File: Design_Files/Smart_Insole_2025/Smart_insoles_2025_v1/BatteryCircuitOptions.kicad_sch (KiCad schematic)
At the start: 2 parts, among them J2 Conn_01x02_Pin

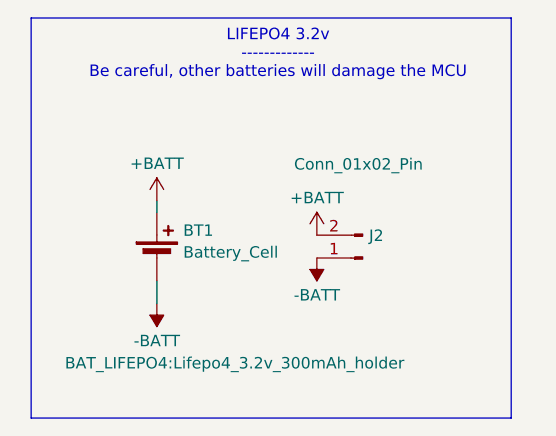
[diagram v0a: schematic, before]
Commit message: Added different AFE circuits to the schematic. Needs verification
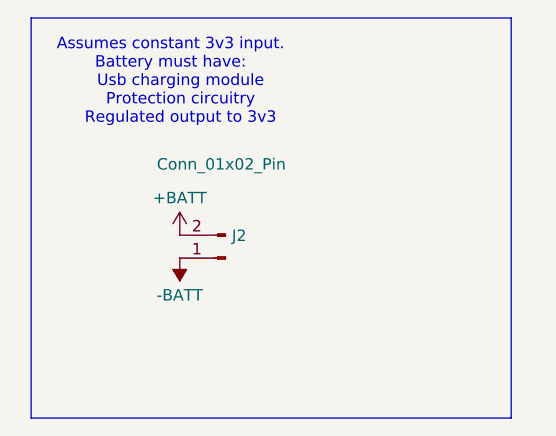
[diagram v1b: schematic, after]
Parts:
- removed BT1: Battery_Cell, BAT_LIFEPO4:Lifepo4_3.2v_300mAh_holder, symbol Device:Battery_Cell
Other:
- note added: "Assumes constant 3v3 input. Battery must have: Usb charging module Protection circuitry Regulated output to 3v3"
- note removed: "LIFEPO4 3.2v ------------- Be careful, other batteries will damage the MCU"
- moved on the sheet: J2

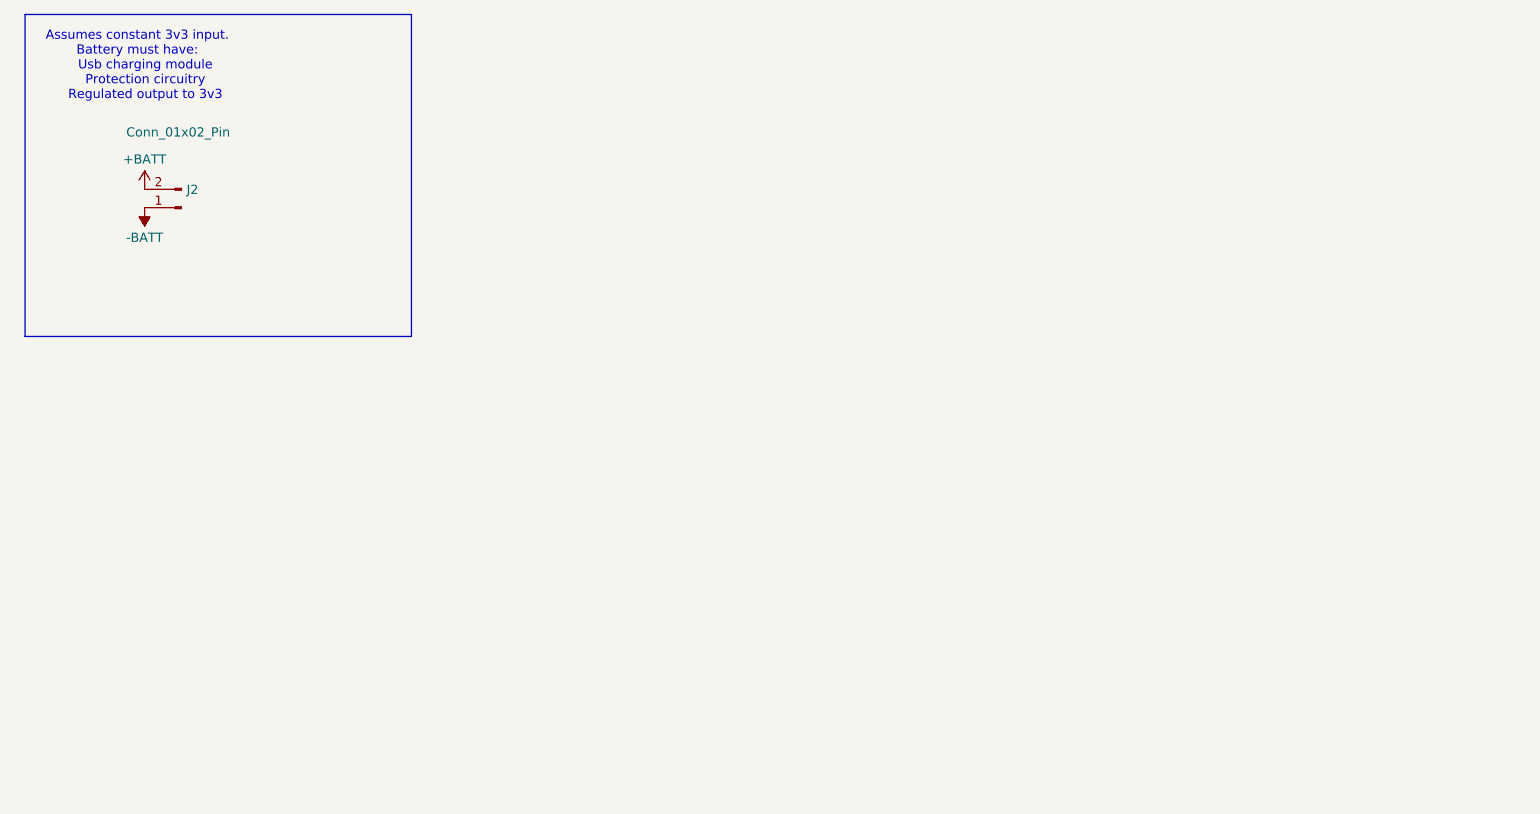
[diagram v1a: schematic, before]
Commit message: Project division to account for multiple AFE conditioning circuit
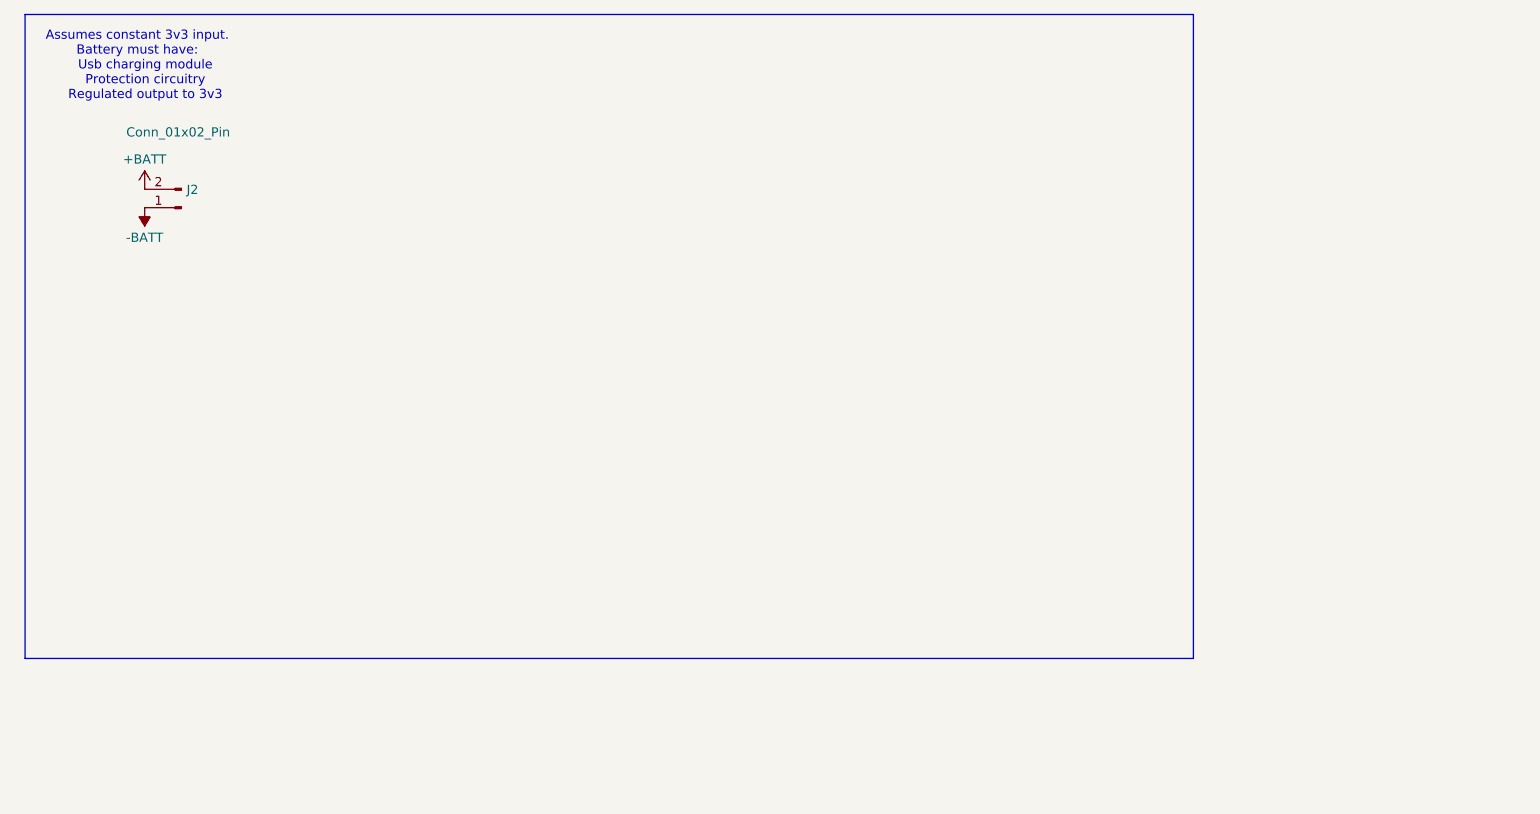
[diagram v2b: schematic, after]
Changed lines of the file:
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@@
 	(rectangle
 		(start 24.13 19.05)
-		(end 77.47 63.5)
+		(end 185.42 107.95)
 		(stroke
 			(width 0)

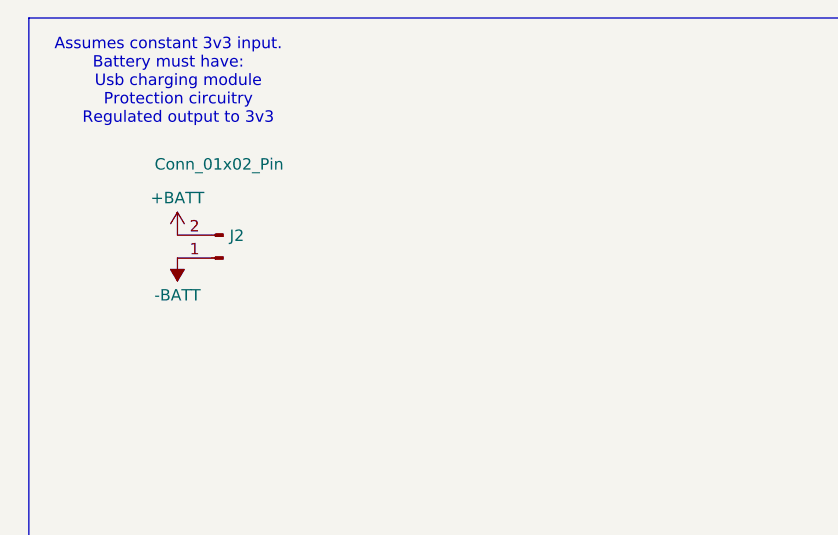
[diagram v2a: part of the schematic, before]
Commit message: Added battery connector footprint. Grouping componnets in PcbNew
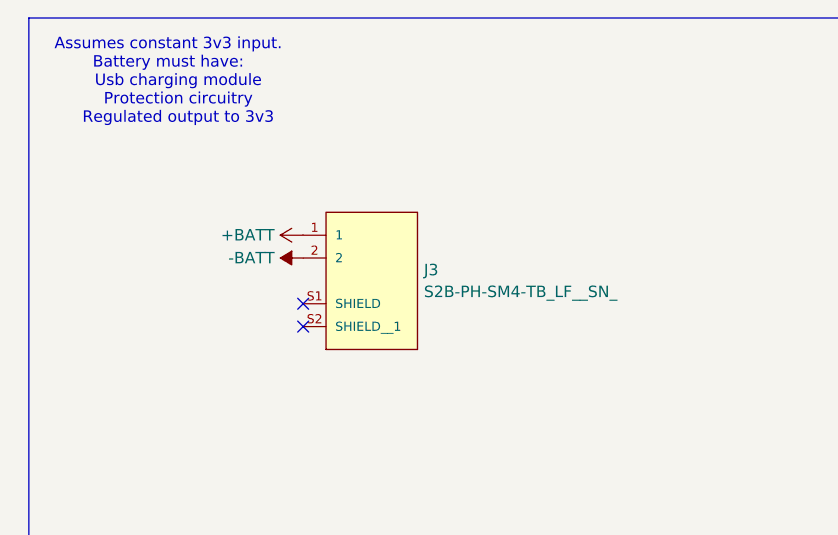
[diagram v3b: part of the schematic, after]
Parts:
- removed J2: Conn_01x02_Pin, Connector_JST:JST_EH_S2B-EH_1x02_P2.50mm_Horizontal, symbol Connector:Conn_01x02_Pin
- added J3: S2B-PH-SM4-TB_LF__SN_, JST-PH2-2.00MM-SMD-HORIZONTAL:JST_S2B-PH-SM4-TB_LF__SN_, symbol S2B-PH-SM4-TB_LF__SN_:S2B-PH-SM4-TB_LF__SN_
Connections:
- net +BATT: now also J3.1
- net -BATT: now also J3.2
- no-connect marks 0 -> 2
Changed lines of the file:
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@@
 	(generator_version "8.0")
 	(paper "A4")
+	(no_connect
+		(at 54.61 50.8)
+	)
+	(no_connect
+		(at 54.61 53.34)
+	)
 	(rectangle
 		(start 24.13 19.05)
@@
 	)
 	(symbol
-		(lib_id "Connector:Conn_01x02_Pin")
-		(at 45.72 45.72 180)
+		(lib_id "power:+BATT")
+		(at 54.61 43.18 90)
 		(unit 1)
 		(exclude_from_sim no)
@@
 		(on_board yes)
 		(dnp no)
-		(property "Reference" "J2"
-			(at 46.4312 43.2378 0)
-			(effects
-				(font
-					(size 1.27 1.27)
-				)
-				(justify right)
-			)
-		)
-		(property "Value" "Conn_01x02_Pin"
-			(at 38.1 35.306 0)
-			(effects
-				(font
-					(size 1.27 1.27)
-				)
-				(justify right)
-			)
-		)
-		(property "Footprint" "Connector_JST:JST_EH_S2B-EH_1x02_P2.50mm_Horizontal"
-			(at 45.72 45.72 0)
-			(effects
-				(font
-					(size 1.27 1.27)
-				)
-				(hide yes)
-			)
-		)
-		(property "Datasheet" "~"
-			(at 45.72 45.72 0)
-			(effects
-				(font
-					(size 1.27 1.27)
-				)
-				(hide yes)
-			)
-		)
-		(property "Description" "Generic connector, single row, 01x02, script generated"
-			(at 45.72 45.72 0)
+		(fields_autoplaced yes)
+		(property "Reference" "#PWR022"
+			(at 58.42 43.18 0)
+			(effects
+				(font
+					(size 1.27 1.27)
+				)
+				(hide yes)
+			)
+		)
+		(property "Value" "+BATT"
+			(at 51.435 43.18 90)
+			(effects
+				(font
+					(size 1.27 1.27)
+				)
+				(justify left)
+			)
+		)
+		(property "Footprint" ""
+			(at 54.61 43.18 0)
+			(effects
+				(font
+					(size 1.27 1.27)
+				)
+				(hide yes)
+			)
+		)
+		(property "Datasheet" ""
+			(at 54.61 43.18 0)
+			(effects
+				(font
+					(size 1.27 1.27)
+				)
+				(hide yes)
+			)
+		)
+		(property "Description" "Power symbol creates a global label with name \"+BATT\""
+			(at 54.61 43.18 0)
 			(effects
 				(font
@@
 		)
 		(pin "1"
-		)
-		(pin "2"
 		)
 		(instances
 			(project "Smart_insoles_2025_v1"
 				(path "/f1f3d712-154d-4111-a7c4-f47541abccf8/720d2e8f-49b8-46ab-8d82-07d24ffc5c73"
-					(reference "J2")
+					(reference "#PWR022")
 					(unit 1)
 				)
@@
 	(symbol
 		(lib_id "power:-BATT")
-		(at 40.64 45.72 180)
+		(at 54.61 45.72 90)
 		(unit 1)
 		(exclude_from_sim no)
@@
 		(fields_autoplaced yes)
 		(property "Reference" "#PWR023"
-			(at 40.64 41.91 0)
+			(at 58.42 45.72 0)
 			(effects
 				(font
@@
 		)
 		(property "Value" "-BATT"
-			(at 40.64 49.8531 0)
-			(effects
-				(font
-					(size 1.27 1.27)
-				)
+			(at 51.435 45.72 90)
+			(effects
+				(font
+					(size 1.27 1.27)
+				)
+				(justify left)
 			)
 		)
 		(property "Footprint" ""
-			(at 40.64 45.72 0)
+			(at 54.61 45.72 0)
 			(effects
 				(font
@@
 		)
 		(property "Datasheet" ""
-			(at 40.64 45.72 0)
+			(at 54.61 45.72 0)
 			(effects
 				(font
@@
 		)
 		(property "Description" "Power symbol creates a global label with name \"-BATT\""
-			(at 40.64 45.72 0)
+			(at 54.61 45.72 0)
 			(effects
 				(font
@@
 	)
 	(symbol
-		(lib_id "power:+BATT")
-		(at 40.64 43.18 0)
+		(lib_id "S2B-PH-SM4-TB_LF__SN_:S2B-PH-SM4-TB_LF__SN_")
+		(at 62.23 45.72 0)
 		(unit 1)
 		(exclude_from_sim no)
@@
 		(dnp no)
 		(fields_autoplaced yes)
-		(property "Reference" "#PWR022"
-			(at 40.64 46.99 0)
-			(effects
-				(font
-					(size 1.27 1.27)
-				)
-				(hide yes)
-			)
-		)
-		(property "Value" "+BATT"
-			(at 40.64 39.0469 0)
-			(effects
-				(font
-					(size 1.27 1.27)
-				)
-			)
-		)
-		(property "Footprint" ""
-			(at 40.64 43.18 0)
-			(effects
-				(font
-					(size 1.27 1.27)
-				)
+		(property "Reference" "J3"
+			(at 68.0212 47.0478 0)
+			(effects
+				(font
+					(size 1.27 1.27)
+				)
+				(justify left)
+			)
+		)
+		(property "Value" "S2B-PH-SM4-TB_LF__SN_"
+			(at 68.0212 49.4721 0)
+			(effects
+				(font
+					(size 1.27 1.27)
+				)
+				(justify left)
+			)
+		)
+		(property "Footprint" "JST-PH2-2.00MM-SMD-HORIZONTAL:JST_S2B-PH-SM4-TB_LF__SN_"
+			(at 62.23 45.72 0)
+			(effects
+				(font
+					(size 1.27 1.27)
+				)
+				(justify bottom)
 				(hide yes)
 			)
 		)
 		(property "Datasheet" ""
-			(at 40.64 43.18 0)
-			(effects
-				(font
-					(size 1.27 1.27)
-				)
-				(hide yes)
-			)
-		)
-		(property "Description" "Power symbol creates a global label with name \"+BATT\""
-			(at 40.64 43.18 0)
-			(effects
-				(font
-					(size 1.27 1.27)
-				)
+			(at 62.23 45.72 0)
+			(effects
+				(font
+					(size 1.27 1.27)
+				)
+				(hide yes)
+			)
+		)
+		(property "Description" ""
+			(at 62.23 45.72 0)
+			(effects
+				(font
+					(size 1.27 1.27)
+				)
+				(hide yes)
+			)
+		)
+		(property "MF" "JST Sales"
+			(at 62.23 45.72 0)
+			(effects
+				(font
+					(size 1.27 1.27)
+				)
+				(justify bottom)
+				(hide yes)
+			)
+		)
+		(property "Description_1" "\n                        \n                            Connector Header Surface Mount, Right Angle 2 position 0.079 (2.00mm)\n                        \n"
+			(at 62.23 45.72 0)
+			(effects
+				(font
+					(size 1.27 1.27)
+				)
+				(justify bottom)
+				(hide yes)
+			)
+		)
+		(property "Package" "None"
+			(at 62.23 45.72 0)
+			(effects
+				(font
+					(size 1.27 1.27)
+				)
+				(justify bottom)
+				(hide yes)
+			)
+		)
+		(property "Price" "None"
+			(at 62.23 45.72 0)
+			(effects
+				(font
+					(size 1.27 1.27)
+				)
+				(justify bottom)
+				(hide yes)
+			)
+		)
+		(property "Check_prices" "https://www.snapeda.com/parts/S2B-PH-SM4-TB(LF)(SN)/JST/view-part/?ref=eda"
+			(at 62.23 45.72 0)
+			(effects
+				(font
+					(size 1.27 1.27)
+				)
+				(justify bottom)
+				(hide yes)
+			)
+		)
+		(property "STANDARD" "Manufacturer Recommendation"
+			(at 62.23 45.72 0)
+			(effects
+				(font
+					(size 1.27 1.27)
+				)
+				(justify bottom)
+				(hide yes)
+			)
+		)
+		(property "SnapEDA_Link" "https://www.snapeda.com/parts/S2B-PH-SM4-TB(LF)(SN)/JST/view-part/?ref=snap"
+			(at 62.23 45.72 0)
+			(effects
+				(font
+					(size 1.27 1.27)
+				)
+				(justify bottom)
+				(hide yes)
+			)
+		)
+		(property "MP" "S2B-PH-SM4-TB(LF)(SN)"
+			(at 62.23 45.72 0)
+			(effects
+				(font
+					(size 1.27 1.27)
+				)
+				(justify bottom)
+				(hide yes)
+			)
+		)
+		(property "Availability" "In Stock"
+			(at 62.23 45.72 0)
+			(effects
+				(font
+					(size 1.27 1.27)
+				)
+				(justify bottom)
+				(hide yes)
+			)
+		)
+		(property "MANUFACTURER" "JST"
+			(at 62.23 45.72 0)
+			(effects
+				(font
+					(size 1.27 1.27)
+				)
+				(justify bottom)
 				(hide yes)
 			)
 		)
 		(pin "1"
+		)
+		(pin "2"
+		)
+		(pin "S2"
+		)
+		(pin "S1"
 		)
 		(instances
 			(project "Smart_insoles_2025_v1"
 				(path "/f1f3d712-154d-4111-a7c4-f47541abccf8/720d2e8f-49b8-46ab-8d82-07d24ffc5c73"
-					(reference "#PWR022")
+					(reference "J3")
 					(unit 1)
 				)

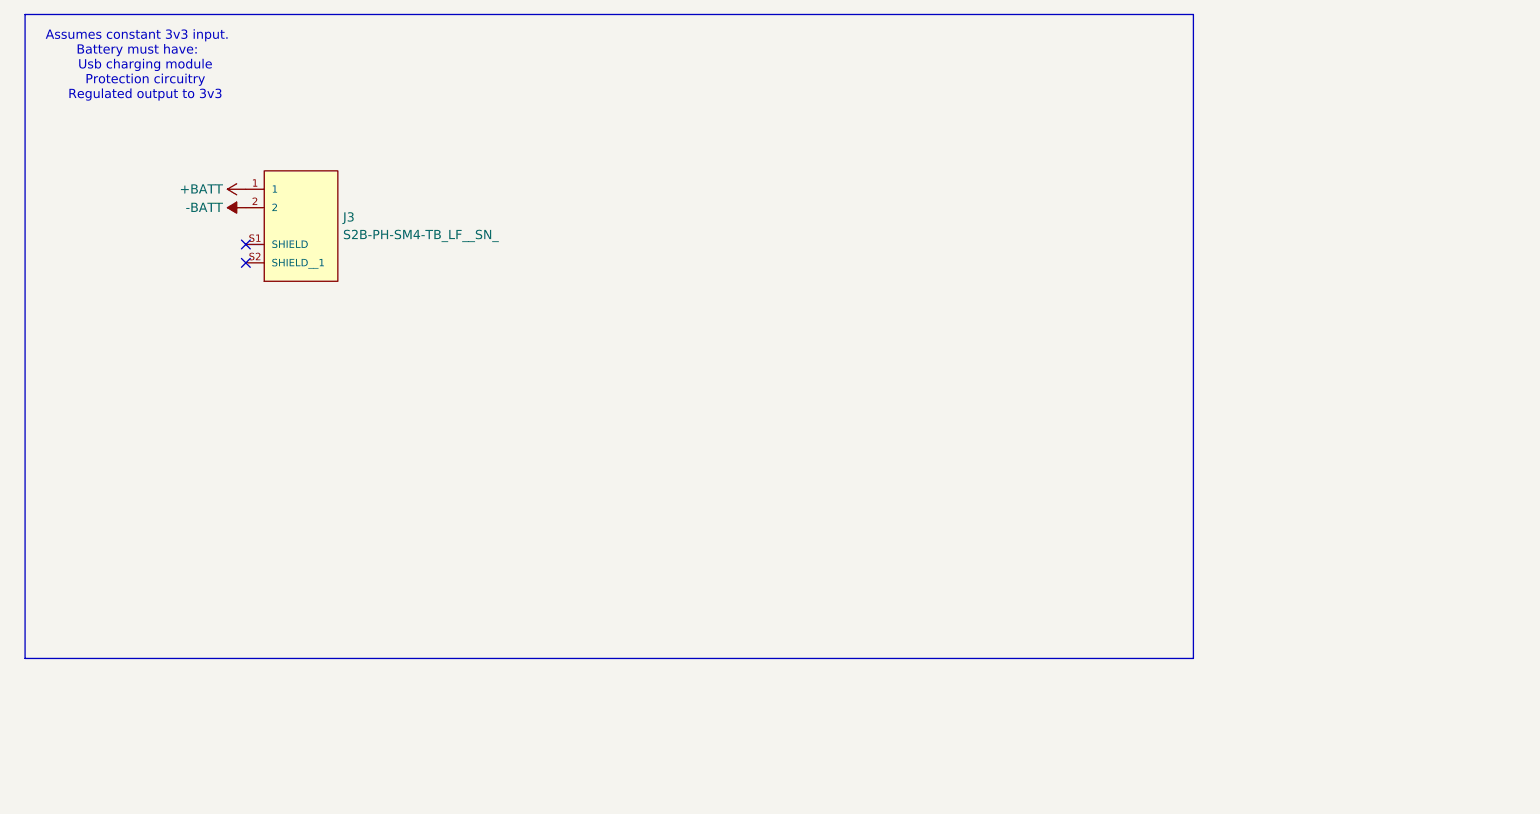
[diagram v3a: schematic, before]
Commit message: PCBnew:Moving placed components. Fixed REF of mcp component
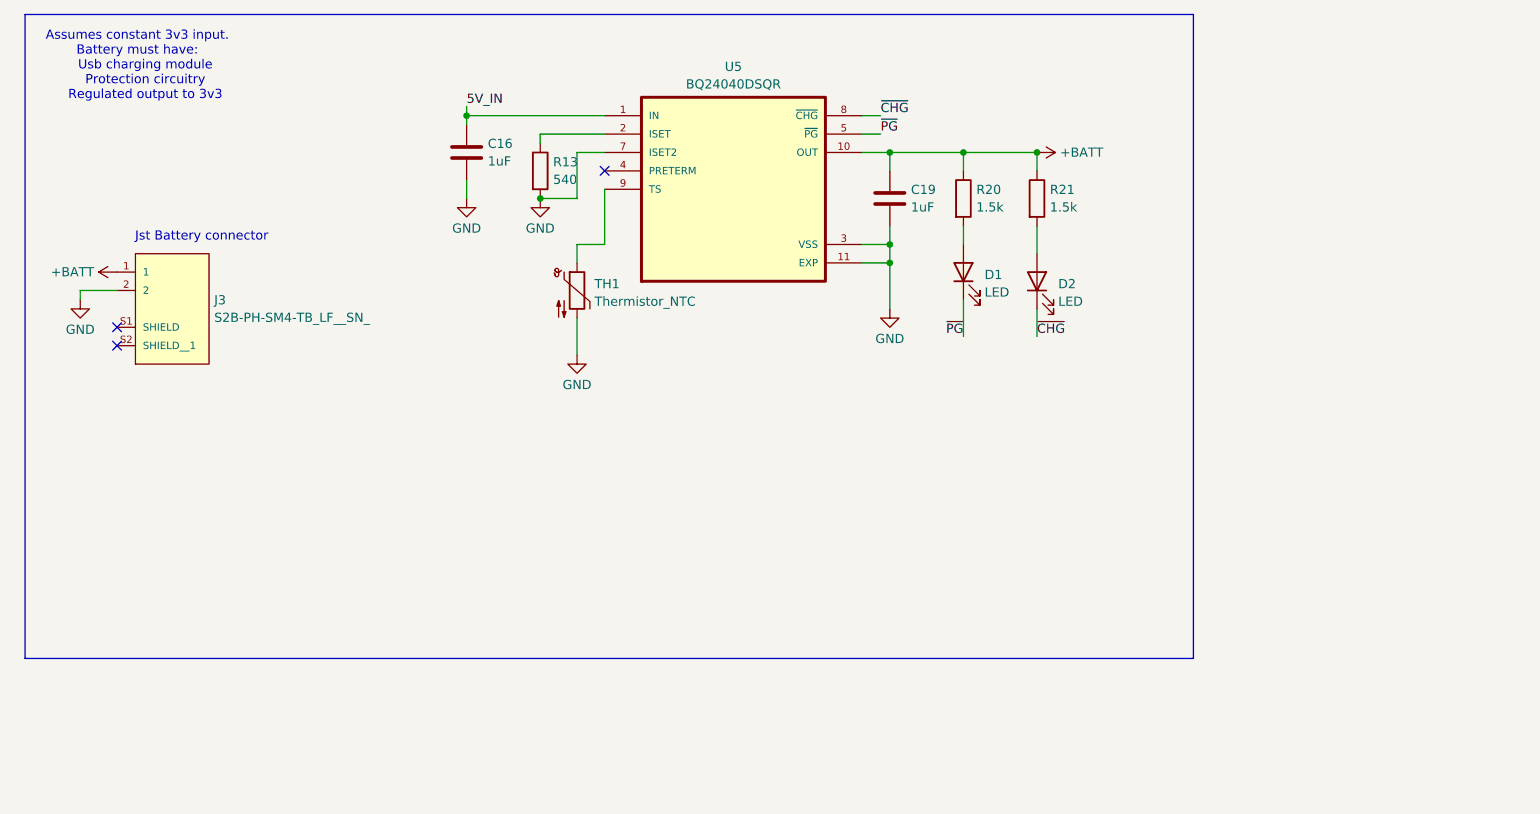
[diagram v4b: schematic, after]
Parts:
- added C16, C19: 1uF, Capacitor_SMD:C_0603_1608Metric, symbol Device:C
- added D1, D2: LED, LED_SMD:LED_0603_1608Metric, symbol Device:LED
- added R13: 540, Resistor_SMD:R_0603_1608Metric, symbol Device:R
- added R20, R21: 1.5k, Resistor_SMD:R_0603_1608Metric, symbol Device:R
- added TH1: Thermistor_NTC, symbol Device:Thermistor_NTC
- added U5: BQ24040DSQR, BQ24040DSQR:SON40P200X200X80-11N, symbol BQ24040DSQR:BQ24040DSQR
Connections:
- net +BATT: now also C19.2, R20.1, R21.1, U5.10 (OUT)
- net -BATT renamed GND
- net GND: now also C16.1, C19.1, R13.2, TH1.2, U5.11 (EXP), U5.3 (VSS), U5.7 (ISET2)
- new net: R13.1, U5.2 (ISET)
- new net: D1.2 (A), R20.2
- new net: D2.2 (A), R21.2
- new net: TH1.1, U5.9 (TS)
- new net 5V_IN: C16.2, U5.1 (IN)
- new net ~{CHG}: D2.1 (K), U5.8 (~{CHG})
- new net ~{PG}: D1.1 (K), U5.5 (~{PG})
- no-connect marks 2 -> 3
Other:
- note added: "Jst Battery connector"
- moved on the sheet: J3
